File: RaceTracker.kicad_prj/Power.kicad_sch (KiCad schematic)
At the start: 40 parts, among them J1 USB-C Sink, J7 LiPo, Q2 SIA817, Q3 2N7002, U3 AP2112K-3.3 -> +3V3D, U5 BQ24195L, U6 AP2112K-3.3 -> +3V3

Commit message: Zwei kritische Schaltplanfehler behoben
Power.kicad_sch: Vertikale GND-Busleitung bei x=20.32 (y=41.91–59.69)
entfernt, die J1.CC1 und J1.CC2 direkt auf GND kurzschloss. Die
Pull-Down-Widerstände R37/R38 (5,1 kΩ) waren damit elektrisch wirkungslos.
Ersetzt durch horizontale Verbindung (12.7, 41.91)→(20.32, 41.91) mit
eigenem GND-Symbol (#PWR042) für J1.GND.

Sensors_Storage.kicad_sch: Vertikale Leitung bei x=20.32 (y=50.8–77.47)
entfernt, die U7.AD0, U7.INT, U7.FSYNC und U7.CLKIN auf GND kurzschloss
und damit IMU_INT (PA10 des SAMD21) dauerhaft auf LOW zog. Ersetzt durch
drei kurze Leitungen mit separaten GND-Symbolen (#PWR100, #PWR101).

Co-Authored-By: Claude Sonnet 4.6 <noreply@anthropic.com>
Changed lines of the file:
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@@
 	(wire
 		(pts
-			(xy 20.32 41.91) (xy 20.32 59.69)
+			(xy 12.7 41.91) (xy 20.32 41.91)
 		)
 		(stroke
@@
 					(unit 1)
 				)
+			)
+		)
+	)
+	(symbol
+		(lib_id "RaceTracker:GND")
+		(at 12.7 41.91 0)
+		(unit 1)
+		(body_style 1)
+		(exclude_from_sim no)
+		(in_bom no)
+		(on_board no)
+		(in_pos_files yes)
+		(dnp no)
+		(property "Reference" "#PWR042"
+			(at 12.7 48.91 0)
+			(hide yes)
+			(show_name no)
+			(do_not_autoplace no)
+			(effects
+				(font
+					(size 1.27 1.27)
+				)
+			)
+		)
+		(property "Value" "GND"
+			(at 3.7 41.91 0)
+			(show_name no)
+			(do_not_autoplace no)
+			(effects
+				(font
+					(size 1.4 1.4)
+				)
+			)
+		)
+		(property "Footprint" ""
+			(at 12.7 41.91 0)
+			(show_name no)
+			(do_not_autoplace no)
+			(effects
+				(font
+					(size 1.27 1.27)
+				)
+			)
+		)
+		(property "Datasheet" ""
+			(at 12.7 41.91 0)
+			(show_name no)
+			(do_not_autoplace no)
+			(effects
+				(font
+					(size 1.27 1.27)
+				)
+			)
+		)
+		(property "Description" ""
+			(at 12.7 41.91 0)
+			(show_name no)
+			(do_not_autoplace no)
+			(effects
+				(font
+					(size 1.27 1.27)
+				)
+			)
+		)
+		(pin "1"
+		)
+		(instances
+			(project "RaceTracker"
+				(path "/91b37a92-c006-41eb-be41-a2390c5c45b2/48e8423c-d46f-487f-85bb-35381b682ff2"
+					(reference "#PWR042")
+					(unit 1)
+				)

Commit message: ERC auf 0/0: J1.CC2/R38, J7-Draht und PB1/R3 verbunden, VBUS-Cap ergänzt
Echte KiCad-ERC (kicad-cli sch erc) fand 7 Verstöße, alle auf dasselbe
Muster zurückgeführt: ein Bauteil-Pin lag exakt auf einem Draht, aber
ohne Endpunkt-Treffer oder Junction erkannt daher KiCad ihn nicht als
verbunden. Behoben durch Draht-Trimming auf die exakte Pin-Position,
verifiziert per kicad-cli-Netzlisten-Diff (nur die betroffenen Pins
ändern sich, sonst nichts an den 128 Bauteilen):

- Power.kicad_sch: J1.CC2 <-> R38 (5,1k Pulldown) verbunden, gleicher
  Fehlertyp wie der CC1/GND-Kurzschluss aus dem letzten Commit, nur
  diesmal eine offene statt einer kurzgeschlossenen Verbindung
- Power.kicad_sch: J7.BATT+ Draht-Überstand über den Steckerkörper
  hinaus entfernt
- MCU_Radio.kicad_sch: PB1 (Reset-Taster) Pin 6 <-> R3 verbunden
- Power.kicad_sch: C34 (1uF) als VBUS-Entkopplung an J1 ergänzt, war
  direkt am USB-C-Stecker komplett unbestückt

Per Datenblatt (TI BQ24195L, u-blox ZED-F9P) als Fehlalarme der
kicad-happy-Analyse verifiziert, keine Änderung nötig: I2C_SCL/SDA
Spannungsdomäne (SCL/SDA sind Open-Drain), STAT/CE fehlender Pull-up
(STAT hat LED+R23, CE hat bewusst R25 als Pull-down), RTK_STAT/GEO_STAT
(Push-Pull-Ausgänge), CHG_VBUS ohne DC-Pfad (Analyzer modelliert keine
Transistor-Leitpfade, Q2 ist ein Standard-P-FET-Passschalter).

Co-Authored-By: Claude Sonnet 5 <noreply@anthropic.com>
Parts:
- added C34: 1uF VBUS decoupling, symbol RaceTracker:C_GENERIC
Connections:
- net GND: now also C34.2
- net at R38.1: now also J1.CC2
- net at F1.1, J1.VBUS: now also C34.1
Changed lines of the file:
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@@
 	(wire
 		(pts
-			(xy 190.5 40.64) (xy 223.52 40.64)
+			(xy 193.04 40.64) (xy 223.52 40.64)
 		)
 		(stroke
@@
 	(wire
 		(pts
-			(xy 17.78 46.99) (xy 22.86 46.99)
+			(xy 20.32 46.99) (xy 22.86 46.99)
 		)
 		(stroke
@@
 	(wire
 		(pts
+			(xy 17.78 36.83) (xy 17.78 29.21)
+		)
+		(stroke
+			(width 0)
+			(type default)
+		)
+	)
+	(wire
+		(pts
+			(xy 22.86 29.21) (xy 22.86 34.29)
+		)
+		(stroke
+			(width 0)
+			(type default)
+		)
+	)
+	(junction
+		(at 17.78 36.83)
+		(diameter 0)
+		(color 0 0 0 0)
+	)
+	(wire
+		(pts
 			(xy 264.16 48.26) (xy 293.37 48.26)
 		)
@@
 					(unit 1)
 				)
+			)
+		)
+	)
+	(symbol
+		(lib_id "RaceTracker:C_GENERIC")
+		(at 20.32 29.21 0)
+		(unit 1)
+		(body_style 1)
+		(exclude_from_sim no)
+		(in_bom yes)
+		(on_board yes)
+		(in_pos_files yes)
+		(dnp no)
+		(property "Reference" "C34"
+			(at 20.32 24.81 0)
+			(show_name no)
+			(do_not_autoplace no)
+			(effects
+				(font
+					(size 1.5 1.5)
+				)
+			)
+		)
+		(property "Value" "1uF VBUS decoupling"
+			(at 20.32 33.61 0)
+			(show_name no)
+			(do_not_autoplace no)
+			(effects
+				(font
+					(size 1.1 1.1)
+				)
+			)
+		)
+		(property "Footprint" ""
+			(at 20.32 29.21 0)
+			(hide yes)
+			(show_name no)
+			(do_not_autoplace no)
+			(effects
+				(font
+					(size 1.27 1.27)
+				)
+			)
+		)
+		(property "Datasheet" ""
+			(at 20.32 29.21 0)
+			(hide yes)
+			(show_name no)
+			(do_not_autoplace no)
+			(effects
+				(font
+					(size 1.27 1.27)
+				)
+			)
+		)
+		(property "Description" ""
+			(at 20.32 29.21 0)
+			(show_name no)
+			(do_not_autoplace no)
+			(effects
+				(font
+					(size 1.27 1.27)
+				)
+			)
+		)
+		(pin "1"
+		)
+		(pin "2"
+		)
+		(instances
+			(project "RaceTracker"
+				(path "/91b37a92-c006-41eb-be41-a2390c5c45b2/48e8423c-d46f-487f-85bb-35381b682ff2"
+					(reference "C34")
+					(unit 1)
+				)
+			)
+		)
+	)
+	(symbol
+		(lib_id "RaceTracker:GND")
+		(at 22.86 34.29 0)
+		(unit 1)
+		(body_style 1)
+		(exclude_from_sim no)
+		(in_bom no)
+		(on_board no)
+		(in_pos_files yes)
+		(dnp no)
+		(property "Reference" "#PWR102"
+			(at 22.86 41.29 0)
+			(hide yes)
+			(show_name no)
+			(do_not_autoplace no)
+			(effects
+				(font
+					(size 1.27 1.27)
+				)
+			)
+		)
+		(property "Value" "GND"
+			(at 13.86 34.29 0)
+			(show_name no)
+			(do_not_autoplace no)
+			(effects
+				(font
+					(size 1.4 1.4)
+				)
+			)
+		)
+		(property "Footprint" ""
+			(at 22.86 34.29 0)
+			(show_name no)
+			(do_not_autoplace no)
+			(effects
+				(font
+					(size 1.27 1.27)
+				)
+			)
+		)
+		(property "Datasheet" ""
+			(at 22.86 34.29 0)
+			(show_name no)
+			(do_not_autoplace no)
+			(effects
+				(font
+					(size 1.27 1.27)
+				)
+			)
+		)
+		(property "Description" ""
+			(at 22.86 34.29 0)
+			(show_name no)
+			(do_not_autoplace no)
+			(effects
+				(font
+					(size 1.27 1.27)
+				)
+			)
+		)
+		(pin "1"
+		)
+		(instances
+			(project "RaceTracker"
+				(path "/91b37a92-c006-41eb-be41-a2390c5c45b2/48e8423c-d46f-487f-85bb-35381b682ff2"
+					(reference "#PWR102")
+					(unit 1)
+				)

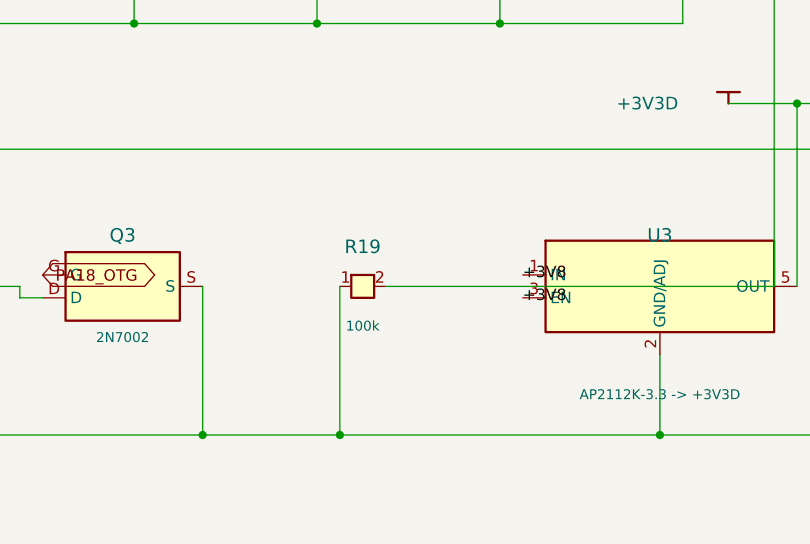
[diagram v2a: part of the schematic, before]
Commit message: Referenzabgleich gegen MKR-WiFi-1010-Eagle-Schaltplan: 2 Abweichungen behoben
Systematischer Netz-für-Netz-Vergleich zwischen der originalen Eagle-
Referenz (MKRWiFi1010V2.0.sch) und der aktuellen KiCad-Netzliste ergab
78 von 85 Netzen exakt identisch. Die restlichen 7 waren bis auf zwei
reine Pin-Namens-/Nummerierungsunterschiede zwischen Eagle- und
KiCad-Symbolen (Q5 Multi-Gate-Split, PB1-Kontaktnummerierung, J7/Q2
Pin-Namen) — keine echten Fehler.

Zwei echte Abweichungen behoben:

- MCU_Radio.kicad_sch: Serienwiderstand R2 (39R) am Reset-Pin des
  SWD-Headers ergänzt. War beim Umbau von MKR-Debug-Header (J2,
  entfallen) auf den neuen SWD-Header (J12) verlorengegangen — SWCLK
  (R4/R12) und SWDIO (R22) hatten ihre Schutzwiderstände behalten,
  nur nRESET nicht. J12.3 hängt jetzt über R2 am RESETN-Netz statt
  direkt.
- Power.kicad_sch: Label "VIN" am Netz R19.2/Q2.Gate/Q2.Anode wieder
  ergänzt (elektrisch war die Verbindung bereits korrekt, nur ohne
  Beschriftung als automatisch benanntes Netz sichtbar).

Beide Änderungen per kicad-cli-Netzlisten-Diff verifiziert (nur die
vier betroffenen Pins ändern sich), ERC weiterhin 0 Fehler/0 Warnungen.

Co-Authored-By: Claude Sonnet 5 <noreply@anthropic.com>
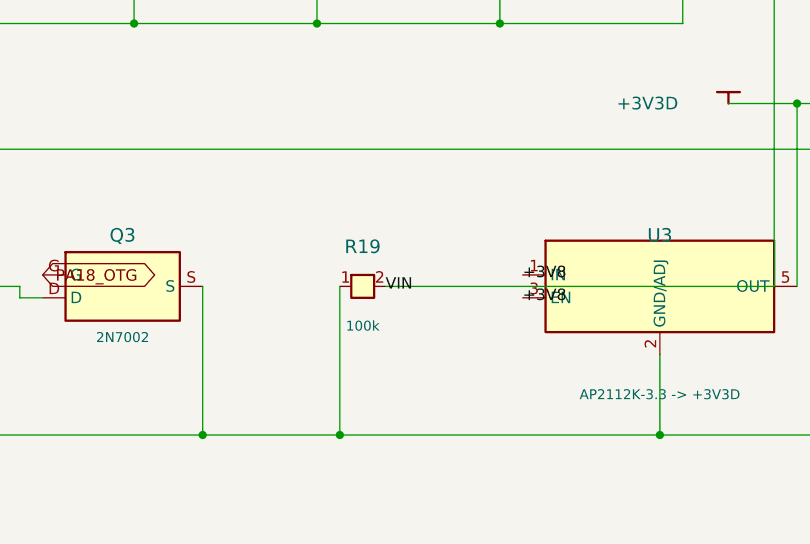
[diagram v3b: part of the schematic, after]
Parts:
- D1: MPN (none) -> PRTR5V0U2X,215; Manufacturer (none) -> NXP
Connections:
- net VIN: now reaches Q2.A, Q2.G, R19.2
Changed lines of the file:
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@@
+			)
+		)
+		(property "Manufacturer" "NXP" (at 0 0 0)
+			(effects
+				(font
+					(size 1.27 1.27)
+				)
+				(hide yes)
+			)
+		)
+		(property "MPN" "PRTR5V0U2X,215" (at 0 0 0)
+			(effects
+				(font
+					(size 1.27 1.27)
+				)
+				(hide yes)
 			)
 		)
@@
 		)
 	)
+	(label "VIN"
+		(at 220.98 152.4 0)
+		(effects
+			(font
+				(size 1.27 1.27)
+			)
+			(justify left)
+		)
+	)

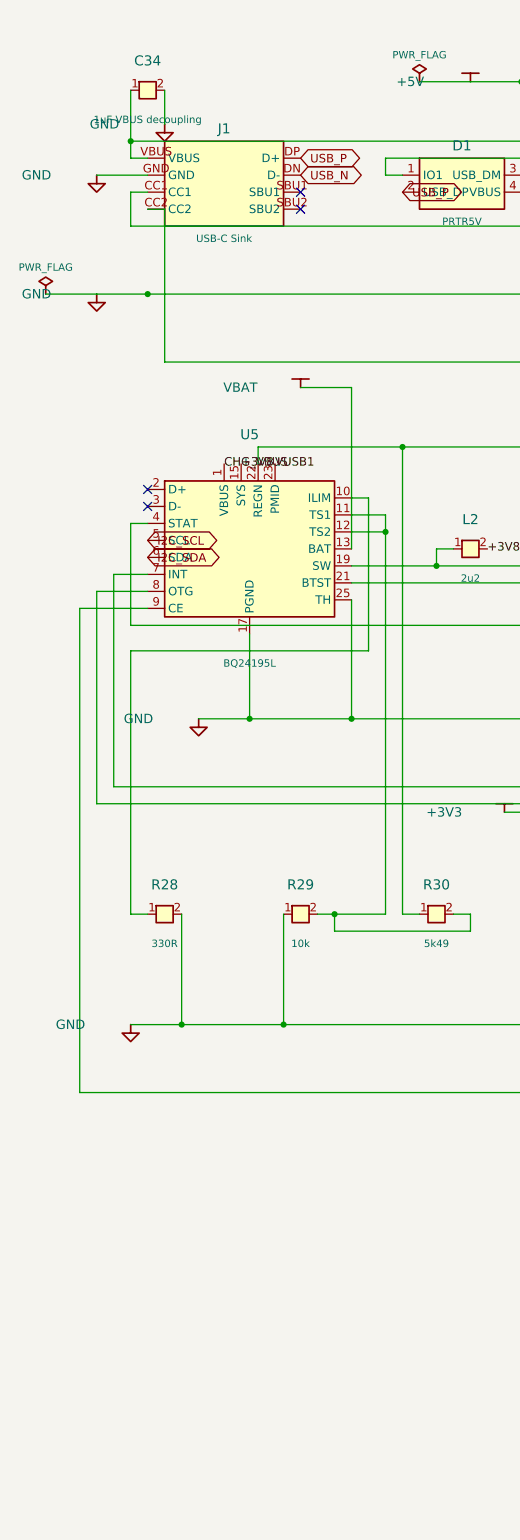
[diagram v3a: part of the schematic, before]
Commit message: J1: echten USB-C-Steckverbinder statt Platzhalter eingebaut
Ersetzt das custom RaceTracker:CONN_USB_C_UFP (8 abstrahierte Pins,
Footprint-Platzhalter TBD_USBC_CONNECTOR) durch KiCads offizielles
Connector_USB:USB_C_Receptacle_USB2.0_16P-Symbol (16 Pins, reales
A/B-Pinout) mit passendem Footprint für einen konkreten, gut verfügbaren
Steckverbinder:

- MPN: TYPE-C-31-M-12 (Hroparts), LCSC C165948, 336k Stück verfügbar
- Footprint: Connector_USB:USB_C_Receptacle_HRO_TYPE-C-31-M-12
  (Pad-Namen A1..B12/SH stimmen exakt mit den Symbol-Pins überein)
- Symboldefinition sowohl im Schaltplan-Cache als auch in
  RaceTracker.kicad_sym ergänzt (nicht nur eingebettet)

Verdrahtung: VBUS (A4/A9/B4/B9) und GND (A1/A12/B1/B12) sind im neuen
Symbol bereits pin-intern zusammengelegt. D+ (A6/B6) und D- (A7/B7)
sind beim USB2.0-Symbol zwei eigenständige Pins und wurden über
globale Labels "USB_P"/"USB_N" gebrückt (verbindet weiterhin korrekt
zu U1 auf MCU_Radio). CC1/CC2 bleiben getrennt (Kabel-Orientierung).
SBU1/SBU2 mit No-Connect-Flag markiert, wie im Original ungenutzt.
GND und SH über zwei neue Massesymbole (#PWR103, #PWR104) angebunden.

Per kicad-cli-Netzlisten-Diff verifiziert: außer J1 selbst ändern sich
nur 4 Netz-Namen (vorher automatisch generiert, jetzt sprechend), keine
Topologie-Änderung. ERC weiterhin 0 Fehler/0 Warnungen.

Co-Authored-By: Claude Sonnet 5 <noreply@anthropic.com>
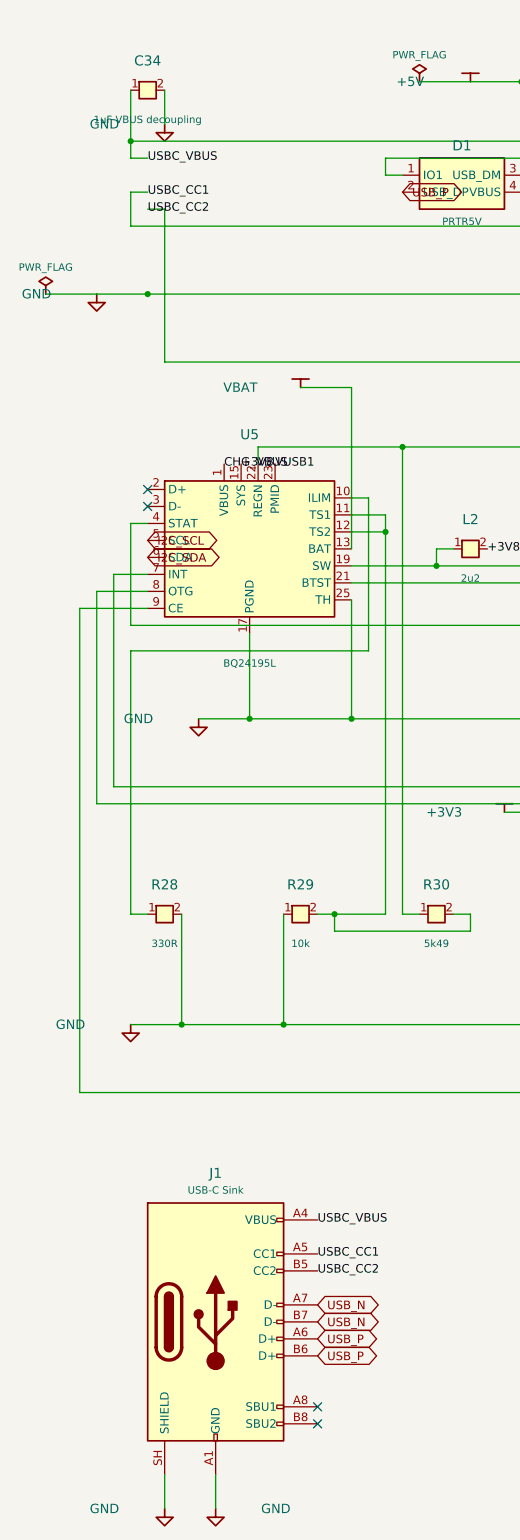
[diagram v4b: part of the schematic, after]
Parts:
- removed J1: USB-C Sink, symbol RaceTracker:CONN_USB_C_UFP
- added J1: USB-C Sink, Connector_USB:USB_C_Receptacle_HRO_TYPE-C-31-M-12, symbol RaceTracker:USB_C_Receptacle_USB2.0_16P
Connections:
- net +5V: now also J1.A7 (D-), J1.B7 (D-)
- net GND: now also J1.A1 (GND), J1.A12 (GND), J1.B1 (GND), J1.B12 (GND), J1.SH (SHIELD)
- net USB_P: now also J1.A6 (D+), J1.B6 (D+)
- net USBC_CC1: now reaches R37.1
- net USBC_CC1: now also J1.A5 (CC1)
- net USBC_CC2: now reaches R38.1
- net USBC_CC2: now also J1.B5 (CC2)
- net USBC_VBUS: now reaches C34.1, F1.1
- net USBC_VBUS: now also J1.A4 (VBUS), J1.A9 (VBUS), J1.B4 (VBUS), J1.B9 (VBUS)
